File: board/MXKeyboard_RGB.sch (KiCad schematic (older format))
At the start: 0 parts

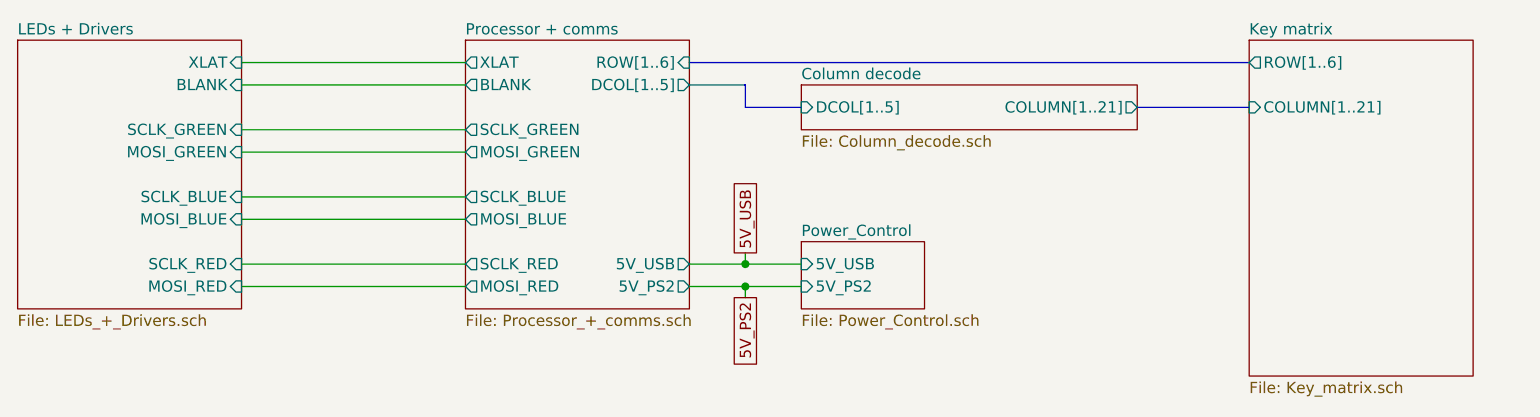
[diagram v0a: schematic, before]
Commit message: Updated the footprints in the schematic having renamed all of my published libraries
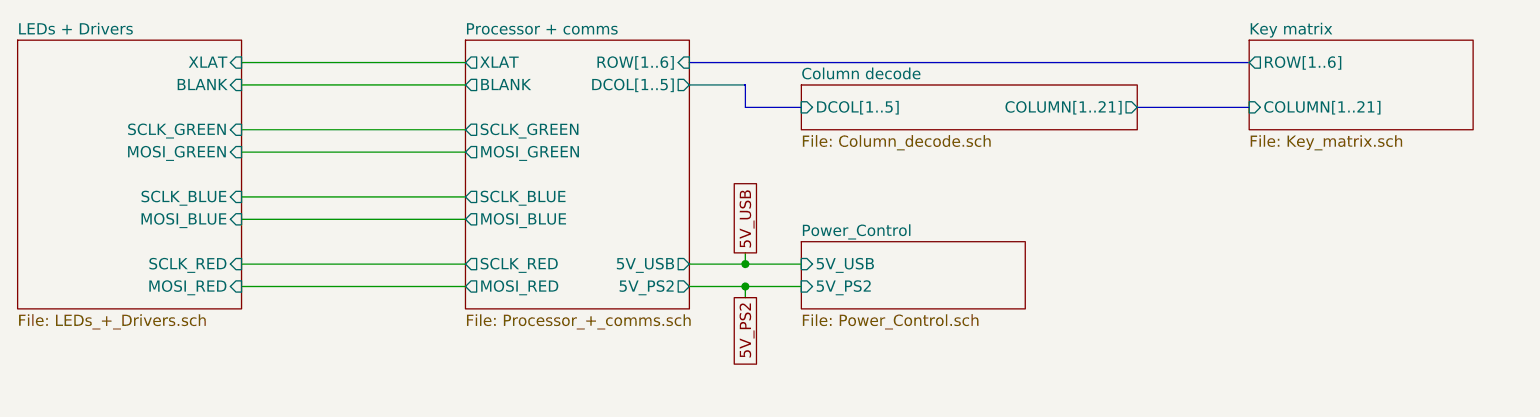
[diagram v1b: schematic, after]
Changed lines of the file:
@@
 $EndDescr
 $Sheet
-S 8000 3500 1000 1500
+S 8000 3500 1000 400
 U 5F5D4893
 F0 "Key matrix" 50
@@
 $EndSheet
 $Sheet
-S 6000 4400 550  300
+S 6000 4400 1000 300
 U 5F5D6721
 F0 "Power_Control" 50

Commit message: Fixed some ERC issues
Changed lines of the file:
@@
 Wire Bus Line
 	5750 3800 6000 3800
-Text GLabel 5750 4450 1    50   UnSpc ~ 0
-5V_USB
 Wire Wire Line
 	5750 4450 5750 4500
@@
 Wire Wire Line
 	5750 4600 5500 4600
-Text GLabel 5750 4650 3    50   UnSpc ~ 0
+Text Label 5750 4450 1    50   ~ 0
+5V_USB
+Text Label 5750 4650 3    50   ~ 0
 5V_PS2
 $EndSCHEMATC

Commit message: Added silkscreen components for the OSH, Tohru (トール) and WEEE logos
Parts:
- added DRG1: トール, トール:トール-12.9x14.8, symbol DX_MON:トール
- added LOGO1: Logo_Open_Hardware_Small, Symbol:OSHW-Logo_11.4x12mm_SilkScreen, symbol Graphic:Logo_Open_Hardware_Small
- added SYM1: SYM_ESD_Large, Symbol:WEEE-Logo_8.4x12mm_SilkScreen, symbol Graphic:SYM_ESD_Large
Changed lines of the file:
@@
 Text Label 5750 4650 3    50   ~ 0
 5V_PS2
+$Comp
+L DX_MON:トール DRG1
+U 1 1 9E88D37C
+P 8000 4450
+F 0 "DRG1" H 8000 4286 60  0001 C CNN
+F 1 "トール" H 8000 4614 60  0001 C CNN
+F 2 "トール:トール-12.9x14.8" H 8000 4450 59  0001 C CNN
+F 3 "" H 8000 4450 59  0001 C CNN
+	1    8000 4450
+	1    0    0    -1
+$EndComp
+$Comp
+L Graphic:Logo_Open_Hardware_Small LOGO1
+U 1 1 9E8917BB
+P 8500 4500
+F 0 "LOGO1" H 8500 4775 50  0001 C CNN
+F 1 "Logo_Open_Hardware_Small" H 8500 4275 50  0001 C CNN
+F 2 "Symbol:OSHW-Logo_11.4x12mm_SilkScreen" H 8500 4500 50  0001 C CNN
+F 3 "~" H 8500 4500 50  0001 C CNN
+	1    8500 4500
+	1    0    0    -1
+$EndComp
+$Comp
+L Graphic:SYM_ESD_Large SYM1
+U 1 1 9E891CAA
+P 9000 4450
+F 0 "SYM1" H 9000 4650 50  0001 C CNN
+F 1 "SYM_ESD_Large" H 9000 4200 50  0001 C CNN
+F 2 "Symbol:WEEE-Logo_8.4x12mm_SilkScreen" H 8995 4420 50  0001 C CNN
+F 3 "~" H 8995 4420 50  0001 C CNN
+	1    9000 4450
+	1    0    0    -1
+$EndComp
 $EndSCHEMATC

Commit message: Cleaned up a bit in the top-level schematic
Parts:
- removed SYM1: SYM_ESD_Large, Symbol:WEEE-Logo_8.4x12mm_SilkScreen, symbol Graphic:SYM_ESD_Large
- DRG1: footprint トール:トール-12.9x14.8 -> トール:トール-34.3x39.5
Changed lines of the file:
@@
 F 0 "DRG1" H 8000 4286 60  0001 C CNN
 F 1 "トール" H 8000 4614 60  0001 C CNN
-F 2 "トール:トール-12.9x14.8" H 8000 4450 59  0001 C CNN
+F 2 "トール:トール-34.3x39.5" H 8000 4450 59  0001 C CNN
 F 3 "" H 8000 4450 59  0001 C CNN
 	1    8000 4450
@@
 	1    0    0    -1
 $EndComp
-$Comp
-L Graphic:SYM_ESD_Large SYM1
-U 1 1 9E891CAA
-P 9000 4450
-F 0 "SYM1" H 9000 4650 50  0001 C CNN
-F 1 "SYM_ESD_Large" H 9000 4200 50  0001 C CNN
-F 2 "Symbol:WEEE-Logo_8.4x12mm_SilkScreen" H 8995 4420 50  0001 C CNN
-F 3 "~" H 8995 4420 50  0001 C CNN
-	1    9000 4450
-	1    0    0    -1
-$EndComp
